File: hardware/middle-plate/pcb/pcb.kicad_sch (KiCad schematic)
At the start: 101 parts, among them J1 Conn_01x06, J2 Conn_01x06, J3 Conn_01x05, J4 Conn_01x04, SW1 MT-0-102-A101-M200-RS+PJ, SW10 TS4535TP 250GF 009, SW11 TS4535TP 250GF 009, SW2 TS4535TP 250GF 009, SW3 TS4535TP 250GF 009, SW4 TS4535TP 250GF 009, SW5 TS4535TP 250GF 009, SW6 TS4535TP 250GF 009, SW7 TS4535TP 250GF 009, SW8 TS4535TP 250GF 009, SW9 TS4535TP 250GF 009, U1 Pico, U2 RPi_Zero_2W, U3 SN74LVC1T45DBV, U4 MAX98357_breakout

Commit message: middle plate completed other than cutouts
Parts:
- added J5: Conn_01x05, Connector_JST:JST_XH_B5B-XH-A_1x05_P2.50mm_Vertical, symbol Connector_Generic:Conn_01x05
- added J6: Conn_01x04, Connector_JST:JST_XH_B4B-XH-A_1x04_P2.50mm_Vertical, symbol Connector_Generic:Conn_01x04
- added JP6, JP7: Jumper_3_Bridged12, Connector_PinHeader_1.27mm:PinHeader_1x03_P1.27mm_Vertical, symbol Jumper:Jumper_3_Bridged12
- added R3, R4: 2.7kR, PCM_Resistor_SMD_AKL:R_1206_3216Metric_Pad1.30x1.75mm_HandSolder, symbol Device:R
- added R5, R6, R7, R8, R9: 10kR, PCM_Resistor_SMD_AKL:R_1206_3216Metric_Pad1.30x1.75mm_HandSolder, symbol Device:R
- added SW12: TS4535TP 250GF 009, EasyEDA:SW-SMD_4P-L4.5-W4.5-P3.00-LS6.8, symbol EasyEDA:TS4535TP250GF009
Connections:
- net +3V3: now also JP6.1 (A), JP7.1 (A), R3.1, R4.1, R5.1, R6.1, R7.1, R8.1, R9.1; no longer U2.17 (3V3)
- net +5V: now also JP6.3 (B), JP7.3 (B)
- net ADC_IN1: now also J5.2 (Pin_2)
- net ADC_IN2: now also J5.4 (Pin_4)
- net ADC_IN3: now also J5.3 (Pin_3)
- net ADC_INT: now also U2.18 (GP24)
- net GND: now also J5.1 (Pin_1), J6.1 (Pin_1), SW12.1, SW12.2
- net IR1: now also U1.22 (GPIO17); no longer U1.1 (GPIO0)
- net IR10: now also U1.2 (GPIO1); no longer U1.12 (GPIO9)
- net IR11: now also U1.4 (GPIO2); no longer U1.14 (GPIO10)
- net IR12: now also U1.5 (GPIO3); no longer U1.15 (GPIO11)
- net IR13: now also U1.6 (GPIO4); no longer U1.16 (GPIO12)
- net IR14: now also U1.7 (GPIO5); no longer U1.17 (GPIO13)
- net IR15: now also U1.9 (GPIO6); no longer U1.19 (GPIO14)
- net IR16: now also U1.10 (GPIO7); no longer U1.20 (GPIO15)
- net IR17: now also U1.11 (GPIO8); no longer U1.34 (GPIO28_ADC2)
- net IR18: now also U1.12 (GPIO9); no longer U1.32 (GPIO27_ADC1)
- net IR19: now also U1.14 (GPIO10); no longer U1.31 (GPIO26_ADC0)
- net IR2: now also U1.21 (GPIO16); no longer U1.2 (GPIO1)
- net IR20: now also U1.15 (GPIO11); no longer U1.29 (GPIO22)
- net IR21: now also U1.16 (GPIO12); no longer U1.27 (GPIO21)
- net IR22: now also U1.17 (GPIO13); no longer U1.26 (GPIO20)
- net IR23: now also U1.19 (GPIO14); no longer U1.25 (GPIO19)
- net IR24: now also U1.20 (GPIO15); no longer U1.24 (GPIO18)
- net IR3: now also U1.24 (GPIO18); no longer U1.4 (GPIO2)
- net IR4: now also U1.25 (GPIO19); no longer U1.5 (GPIO3)
- net IR5: now also U1.26 (GPIO20); no longer U1.6 (GPIO4)
- net IR6: now also U1.27 (GPIO21); no longer U1.7 (GPIO5)
- net IR7: now also U1.32 (GPIO27_ADC1); no longer U1.9 (GPIO6)
- net IR8: now also U1.34 (GPIO28_ADC2); no longer U1.10 (GPIO7)
- net IR9: now also U1.1 (GPIO0); no longer U1.11 (GPIO8)
- net LED_SIG_3V3: now also U1.31 (GPIO26_ADC0); no longer U1.22 (GPIO17)
- net LED_SIG_DIR: now also U1.29 (GPIO22); no longer U1.21 (GPIO16), U2.36 (GP16)
- net LRC: now also U2.16 (GP23); no longer U2.37 (GP26)
- net PI_SW1: now also U2.31 (GP6), R5.2; no longer U2.15 (GP22)
- net PI_SW2: now also U2.29 (GP5), R6.2; no longer U2.27 (GP0(EEPROM_SDA))
- net PI_SW3: now also U2.27 (GP0(EEPROM_SDA)), R7.2; no longer U2.29 (GP5)
- net PI_SW4: now also U2.36 (GP16), R8.2; no longer U2.31 (GP6)
- net PWM0: now also J6.3 (Pin_3)
- net PWM1: now also J6.2 (Pin_2)
- net TOPPICO_TOGGLE.RUN: now reaches U2.7 (GP4(GPCLK0))
- net TOPPICO_TOGGLE.RUN: now also CTRL1.2 (Pin_2), SW3.3, SW3.4
- net BOTTOMPICO_EN renamed TOPPICO_TOGGLE.EN
- net TOPPICO_TOGGLE.EN: now also CTRL1.1 (Pin_1)
- removed net BOTTOMPICO_RUN: SW3.3, SW3.4, U2.13 (GP27)
- removed net EN: CTRL1.1 (Pin_1), CTRL2.2 (Pin_2), U1.37 (3V3_EN)
- net MIDPICO_EN renamed MIDPICO_TOGGLE.EN
- net MIDPICO_TOGGLE.EN: now also U1.37 (3V3_EN)
- net MIDPICO_RUN renamed MIDPICO_TOGGLE.RUN
- net MIDPICO_TOGGLE.RUN: now also U1.30 (RUN)
- net PCM_CLK renamed PCM.CLK
- net PCM_DIN renamed PCM.DIN
- net PCM.DIN: now also J3.2 (Pin_2); no longer J3.4 (Pin_4)
- net PCM_DOUT renamed PCM.DOUT
- net PCM_FS renamed PCM.FS
- net PCM.FS: now also J3.4 (Pin_4); no longer J3.2 (Pin_2)
- removed net RUN: CTRL1.2 (Pin_2), CTRL2.1 (Pin_1), U1.30 (RUN)
- net RX renamed PI_UART.RX
- net PI_UART.RX: now also CTRL2.4 (Pin_4); no longer CTRL2.3 (Pin_3)
- net SCL renamed PI_I2C.SCL
- net PI_I2C.SCL: now also J4.2 (Pin_2), R4.2; no longer J4.3 (Pin_3)
- net SDA renamed PI_I2C.SDA
- net PI_I2C.SDA: now also J4.3 (Pin_3), R3.2; no longer J4.2 (Pin_2)
- net SPI0_CE0 renamed RPI_SPI0.MOSI
- net RPI_SPI0.MOSI: now also J2.5 (Pin_5), U2.19 (GP10(SPI0_MOSI)); no longer U2.24 (GP8(SPI0_CE0))
- net SPI0_CE1 renamed RPI_SPI0.SCS1
- net RPI_SPI0.SCS1: now also J2.2 (Pin_2); no longer J2.5 (Pin_5)
- net SPI0_MISO renamed RPI_SPI0.SCLK
- net RPI_SPI0.SCLK: now also U2.23 (GP11(SPI0_SCLK)); no longer U2.21 (GP9(SPI0_MISO))
- removed net SPI0_MOSI: J1.2 (Pin_2), J2.2 (Pin_2), U2.19 (GP10(SPI0_MOSI))
- net SPI0_SCLK renamed RPI_SPI0.MISO
- net RPI_SPI0.MISO: now also U2.21 (GP9(SPI0_MISO)); no longer U2.23 (GP11(SPI0_SCLK))
- net TOPPICO_EN renamed BOTTOMPICO_TOGGLE.EN
- net BOTTOMPICO_TOGGLE.EN: now also CTRL2.2 (Pin_2), U2.13 (GP27); no longer U2.16 (GP23)
- net TOPPICO_RUN renamed BOTTOMPICO_TOGGLE.RUN
- net BOTTOMPICO_TOGGLE.RUN: now also CTRL2.1 (Pin_1), U2.15 (GP22); no longer U2.18 (GP24)
- net TX renamed PI_UART.TX
- net PI_UART.TX: now also CTRL2.3 (Pin_3); no longer CTRL2.4 (Pin_4)
- new net: J6.4 (Pin_4), JP7.2 (C)
- new net: J5.5 (Pin_5), JP6.2 (C)
- new net PI_SW5: R9.2, SW12.3, SW12.4, U2.37 (GP26)
- new net RPI_SPI0.SCS0: J1.2 (Pin_2), U2.24 (GP8(SPI0_CE0))
- no-connect marks 27 -> 28
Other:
- note added: "A bunch of pushbuttons for centralised hardware and software control. RPi control pushbuttons have a pullup resistor. Make sure it can only sink 0.5mA (at least 7kOhm)."
- note added: "pullup resistors for I2C. Internal pullups of the RPi Zero 2W are too weak to reliably drive 400kHz I2C. Adjust values accordingly, 2.7K is probably safe. DNP and lower speeds if necessary. Lower values can be used if capacitance is too high. And of course, avoid running I2C on wires."
- note removed: "A bunch of pushbuttons for centralised hardware and software control."
- moved on the sheet: CTRL1, CTRL2, H1, H10, H11, H12, H13, H14, H15, H16, H2, H3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

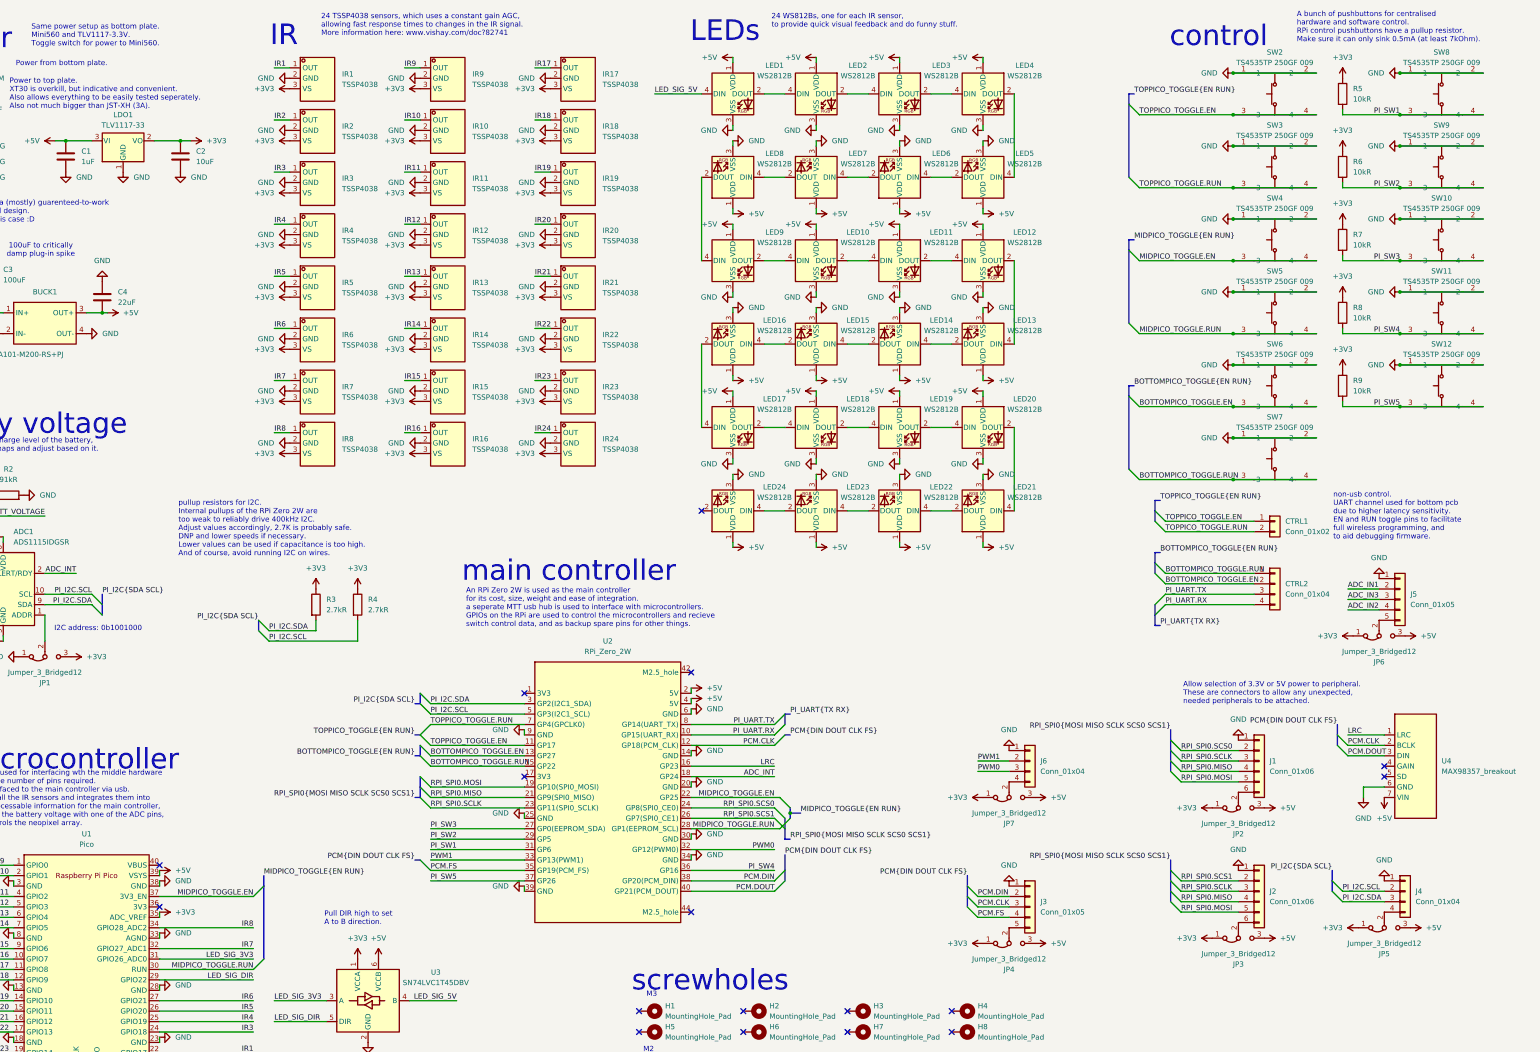
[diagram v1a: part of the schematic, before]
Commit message: changed some reference designators, and cleaned up schematics
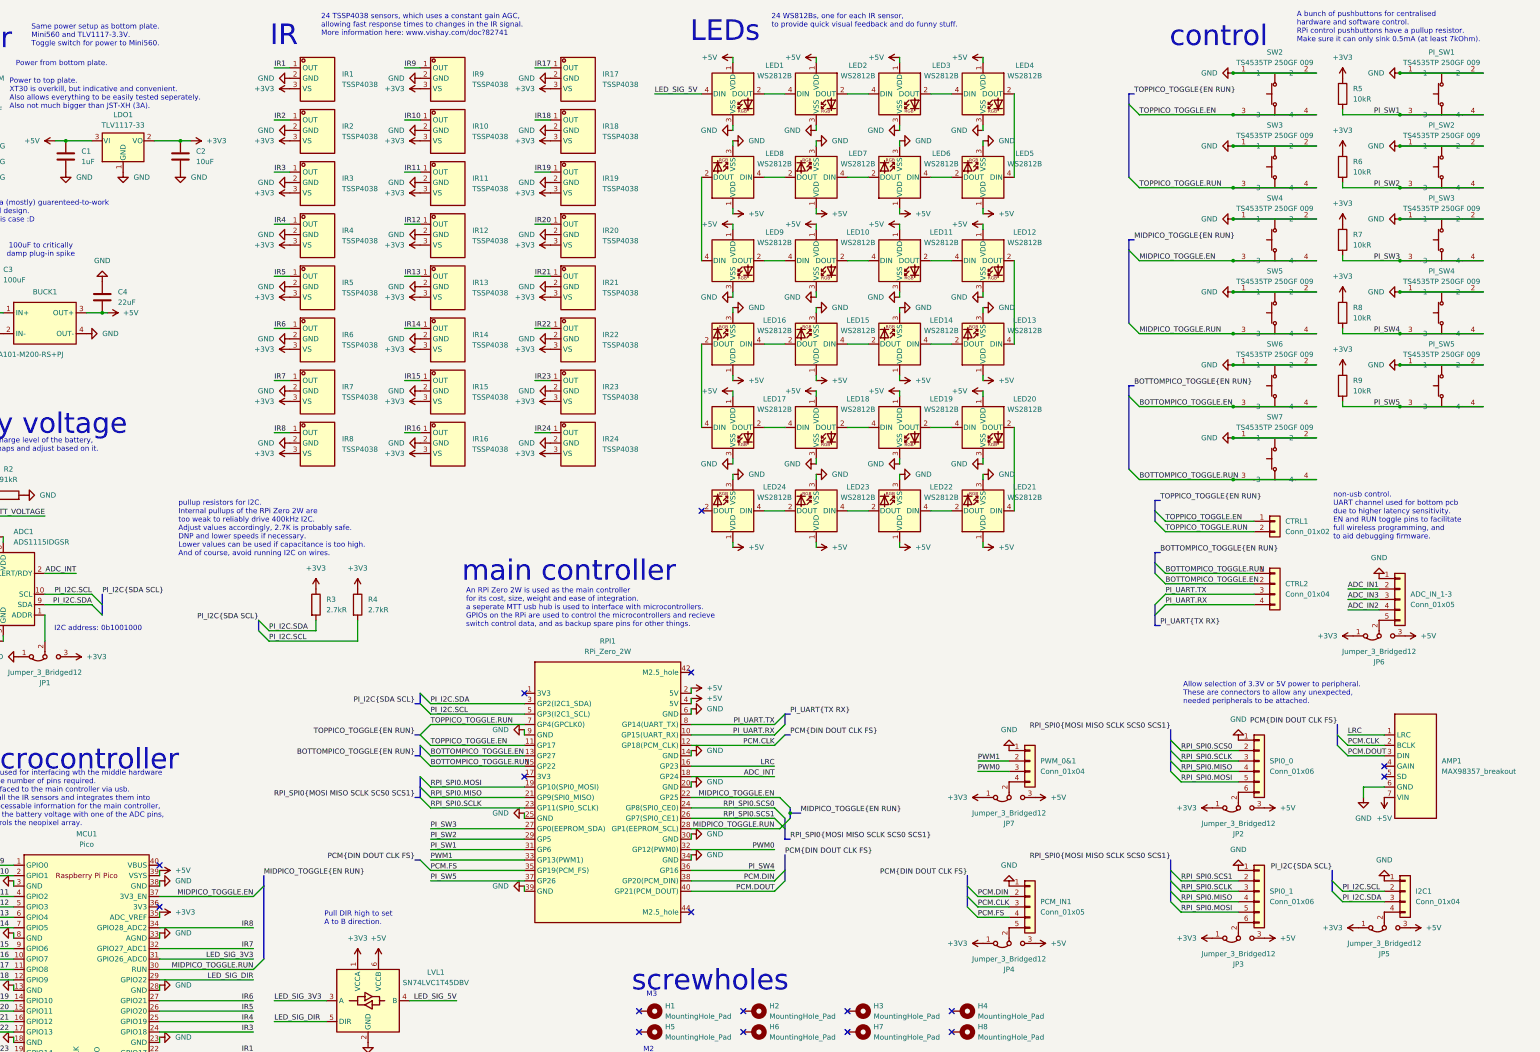
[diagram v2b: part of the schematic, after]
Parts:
- renumbered J5 to ADC_IN_1-3, U4 to AMP1, J4 to I2C1, U3 to LVL1, U1 to MCU1, J3 to PCM_IN1, SW8 to PI_SW1, SW9 to PI_SW2, SW10 to PI_SW3, SW11 to PI_SW4, SW12 to PI_SW5, J6 to PWM_0&1, U2 to RPI1, J1 to SPI0_0, J2 to SPI0_1
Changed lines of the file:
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@@
 		(dnp no)
 		(fields_autoplaced yes)
-		(property "Reference" "U2"
+		(property "Reference" "RPI1"
 			(at 185.42 168.91 0)
 			(effects
@@
 			(project ""
 				(path "/9bb3e9c6-12db-4b47-aa39-b193ca752b9a"
-					(reference "U2")
+					(reference "RPI1")
 					(unit 1)
 				)
@@
 		(dnp no)
 		(fields_autoplaced yes)
-		(property "Reference" "U3"
+		(property "Reference" "LVL1"
 			(at 143.51 249.6055 0)
 			(effects
@@
 			(project "pcb"
 				(path "/9bb3e9c6-12db-4b47-aa39-b193ca752b9a"
-					(reference "U3")
+					(reference "LVL1")
 					(unit 1)
 				)
@@
 		(dnp no)
 		(fields_autoplaced yes)
-		(property "Reference" "U1"
+		(property "Reference" "MCU1"
 			(at 58.42 215.9 0)
 			(effects
@@
 			(project ""
 				(path "/9bb3e9c6-12db-4b47-aa39-b193ca752b9a"
-					(reference "U1")
+					(reference "MCU1")
 					(unit 1)
 				)
@@
 		(dnp no)
 		(fields_autoplaced yes)
-		(property "Reference" "SW12"
+		(property "Reference" "PI_SW5"
 			(at 388.62 96.52 0)
 			(effects
@@
 			(project "pcb"
 				(path "/9bb3e9c6-12db-4b47-aa39-b193ca752b9a"
-					(reference "SW12")
+					(reference "PI_SW5")
 					(unit 1)
 				)
@@
 		(dnp no)
 		(fields_autoplaced yes)
-		(property "Reference" "J6"
+		(property "Reference" "PWM_0&1"
 			(at 290.83 198.1199 0)
 			(effects
@@
 			(project "pcb"
 				(path "/9bb3e9c6-12db-4b47-aa39-b193ca752b9a"
-					(reference "J6")
+					(reference "PWM_0&1")
 					(unit 1)
 				)
@@
 		(dnp no)
 		(fields_autoplaced yes)
-		(property "Reference" "J3"
+		(property "Reference" "PCM_IN1"
 			(at 290.83 232.4099 0)
 			(effects
@@
 			(project ""
 				(path "/9bb3e9c6-12db-4b47-aa39-b193ca752b9a"
-					(reference "J3")
+					(reference "PCM_IN1")
 					(unit 1)
 				)
@@
 		(dnp no)
 		(fields_autoplaced yes)
-		(property "Reference" "J4"
+		(property "Reference" "I2C1"
 			(at 382.27 229.8699 0)
 			(effects
@@
 			(project ""
 				(path "/9bb3e9c6-12db-4b47-aa39-b193ca752b9a"
-					(reference "J4")
+					(reference "I2C1")
 					(unit 1)
 				)
@@
 		(dnp no)
 		(fields_autoplaced yes)
-		(property "Reference" "SW11"
+		(property "Reference" "PI_SW4"
 			(at 388.62 78.74 0)
 			(effects
@@
 			(project "middle-plate"
 				(path "/9bb3e9c6-12db-4b47-aa39-b193ca752b9a"
-					(reference "SW11")
+					(reference "PI_SW4")
 					(unit 1)
 				)
@@
 		(dnp no)
 		(fields_autoplaced yes)
-		(property "Reference" "SW9"
+		(property "Reference" "PI_SW2"
 			(at 388.62 43.18 0)
 			(effects
@@
 			(project "middle-plate"
 				(path "/9bb3e9c6-12db-4b47-aa39-b193ca752b9a"
-					(reference "SW9")
+					(reference "PI_SW2")
 					(unit 1)
 				)
@@
 		(dnp no)
 		(fields_autoplaced yes)
-		(property "Reference" "J1"
+		(property "Reference" "SPI0_0"
 			(at 346.71 198.1199 0)
 			(effects
@@
 			(project ""
 				(path "/9bb3e9c6-12db-4b47-aa39-b193ca752b9a"
-					(reference "J1")
+					(reference "SPI0_0")
 					(unit 1)
 				)
@@
 		(dnp no)
 		(fields_autoplaced yes)
-		(property "Reference" "SW10"
+		(property "Reference" "PI_SW3"
 			(at 388.62 60.96 0)
 			(effects
@@
 			(project "middle-plate"
 				(path "/9bb3e9c6-12db-4b47-aa39-b193ca752b9a"
-					(reference "SW10")
+					(reference "PI_SW3")
 					(unit 1)
 				)
@@
 		(dnp no)
 		(fields_autoplaced yes)
-		(property "Reference" "J2"
+		(property "Reference" "SPI0_1"
 			(at 346.71 229.8699 0)
 			(effects
@@
 			(project "middle-plate"
 				(path "/9bb3e9c6-12db-4b47-aa39-b193ca752b9a"
-					(reference "J2")
+					(reference "SPI0_1")
 					(unit 1)
 				)
@@
 		(dnp no)
 		(fields_autoplaced yes)
-		(property "Reference" "U4"
+		(property "Reference" "AMP1"
 			(at 388.62 198.1199 0)
 			(effects
@@
 			(project ""
 				(path "/9bb3e9c6-12db-4b47-aa39-b193ca752b9a"
-					(reference "U4")
+					(reference "AMP1")
 					(unit 1)
 				)
@@
 		(dnp no)
 		(fields_autoplaced yes)
-		(property "Reference" "SW8"
+		(property "Reference" "PI_SW1"
 			(at 388.62 25.4 0)
 			(effects
@@
 			(project "middle-plate"
 				(path "/9bb3e9c6-12db-4b47-aa39-b193ca752b9a"
-					(reference "SW8")
+					(reference "PI_SW1")
 					(unit 1)
 				)
@@
 		(dnp no)
 		(fields_autoplaced yes)
-		(property "Reference" "J5"
+		(property "Reference" "ADC_IN_1-3"
 			(at 381 157.4799 0)
 			(effects
@@
 			(project "pcb"
 				(path "/9bb3e9c6-12db-4b47-aa39-b193ca752b9a"
-					(reference "J5")
+					(reference "ADC_IN_1-3")
 					(unit 1)
 				)

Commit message: funny thing
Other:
- note added: "What could this sneaky amp be possibly doing? Have any grapes?"
- moved on the sheet: AMP1
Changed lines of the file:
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@@
 	)
 	(no_connect
-		(at 374.65 201.93)
+		(at 261.62 170.18)
 	)
 	(no_connect
@@
 	)
 	(no_connect
-		(at 374.65 199.39)
+		(at 261.62 167.64)
 	)
 	(no_connect
@@
 	)
 	(bus_entry
-		(at 363.22 191.77)
+		(at 250.19 160.02)
 		(size 2.54 2.54)
 		(stroke
@@
 	)
 	(bus_entry
-		(at 363.22 194.31)
+		(at 250.19 162.56)
 		(size 2.54 2.54)
 		(stroke
@@
 	(wire
 		(pts
-			(xy 365.76 196.85) (xy 374.65 196.85)
+			(xy 252.73 165.1) (xy 261.62 165.1)
 		)
 		(stroke
@@
 	(wire
 		(pts
-			(xy 369.57 204.47) (xy 369.57 207.01)
+			(xy 256.54 172.72) (xy 256.54 175.26)
 		)
 		(stroke
@@
 	(bus
 		(pts
-			(xy 363.22 189.23) (xy 363.22 191.77)
+			(xy 250.19 157.48) (xy 250.19 160.02)
 		)
 		(stroke
@@
 	(wire
 		(pts
-			(xy 369.57 204.47) (xy 374.65 204.47)
+			(xy 256.54 172.72) (xy 261.62 172.72)
 		)
 		(stroke
@@
 	(bus
 		(pts
-			(xy 363.22 191.77) (xy 363.22 194.31)
+			(xy 250.19 160.02) (xy 250.19 162.56)
 		)
 		(stroke
@@
 	(wire
 		(pts
-			(xy 365.76 191.77) (xy 374.65 191.77)
+			(xy 252.73 160.02) (xy 261.62 160.02)
 		)
 		(stroke
@@
 	(wire
 		(pts
-			(xy 365.76 194.31) (xy 374.65 194.31)
+			(xy 252.73 162.56) (xy 261.62 162.56)
 		)
 		(stroke
@@
 		)
 	)
+	(text "What could this sneaky\namp be possibly doing?\nHave any grapes?"
+		(exclude_from_sim no)
+		(at 276.098 158.496 0)
+		(effects
+			(font
+				(size 1.27 1.27)
+			)
+			(justify left)
+		)
+	)
 	(text "MINI560 reg, to have a (mostly) guarenteed-to-work\nand replacable-if-fried design.\n5A is not overkill in this case :D"
 		(exclude_from_sim no)
@@
 	)
 	(label "PCM{DIN DOUT CLK FS}"
-		(at 363.22 189.23 180)
+		(at 250.19 157.48 180)
 		(fields_autoplaced yes)
 		(effects
@@
 	)
 	(label "PCM.CLK"
-		(at 365.76 194.31 0)
+		(at 252.73 162.56 0)
 		(fields_autoplaced yes)
 		(effects
@@
 	)
 	(label "LRC"
-		(at 365.76 191.77 0)
+		(at 252.73 160.02 0)
 		(fields_autoplaced yes)
 		(effects
@@
 	)
 	(label "PCM.DOUT"
-		(at 365.76 196.85 0)
+		(at 252.73 165.1 0)
 		(fields_autoplaced yes)
 		(effects
@@
 	(symbol
 		(lib_id "power:GND")
-		(at 369.57 207.01 0)
+		(at 256.54 175.26 0)
 		(unit 1)
 		(exclude_from_sim no)
@@
 		(fields_autoplaced yes)
 		(property "Reference" "#PWR0161"
-			(at 369.57 213.36 0)
+			(at 256.54 181.61 0)
 			(effects
 				(font
@@
 		)
 		(property "Value" "GND"
-			(at 369.57 212.09 0)
+			(at 256.54 180.34 0)
 			(effects
 				(font
@@
 		)
 		(property "Footprint" ""
-			(at 369.57 207.01 0)
+			(at 256.54 175.26 0)
 			(effects
 				(font
@@
 		)
 		(property "Datasheet" ""
-			(at 369.57 207.01 0)
+			(at 256.54 175.26 0)
 			(effects
 				(font
@@
 		)
 		(property "Description" "Power symbol creates a global label with name \"GND\" , ground"
-			(at 369.57 207.01 0)
+			(at 256.54 175.26 0)
 			(effects
 				(font
@@
 	(symbol
 		(lib_id "custom:MAX98357_breakout_no_mountingholes")
-		(at 379.73 199.39 0)
+		(at 266.7 167.64 0)
 		(unit 1)
 		(exclude_from_sim no)
@@
 		(fields_autoplaced yes)
 		(property "Reference" "AMP1"
-			(at 388.62 198.1199 0)
+			(at 275.59 166.3699 0)
 			(effects
 				(font
@@
 		)
 		(property "Value" "MAX98357_breakout"
-			(at 388.62 200.6599 0)
+			(at 275.59 168.9099 0)
 			(effects
 				(font
@@
 		)
 		(property "Footprint" "custom:MAX98357_breakout_no_mountingholes"
-			(at 379.73 199.39 0)
+			(at 266.7 167.64 0)
 			(effects
 				(font
@@
 		)
 		(property "Datasheet" ""
-			(at 379.73 199.39 0)
+			(at 266.7 167.64 0)
 			(effects
 				(font
@@
 		)
 		(property "Description" ""
-			(at 379.73 199.39 0)
+			(at 266.7 167.64 0)
 			(effects
 				(font
@@
 	(symbol
 		(lib_id "power:+5V")
-		(at 374.65 207.01 180)
+		(at 261.62 175.26 180)
 		(unit 1)
 		(exclude_from_sim no)
@@
 		(fields_autoplaced yes)
 		(property "Reference" "#PWR0162"
-			(at 374.65 203.2 0)
+			(at 261.62 171.45 0)
 			(effects
 				(font
@@
 		)
 		(property "Value" "+5V"
-			(at 374.65 212.09 0)
+			(at 261.62 180.34 0)
 			(effects
 				(font
@@
 		)
 		(property "Footprint" ""
-			(at 374.65 207.01 0)
+			(at 261.62 175.26 0)
 			(effects
 				(font
@@
 		)
 		(property "Datasheet" ""
-			(at 374.65 207.01 0)
+			(at 261.62 175.26 0)
 			(effects
 				(font
@@
 		)
 		(property "Description" "Power symbol creates a global label with name \"+5V\""
-			(at 374.65 207.01 0)
+			(at 261.62 175.26 0)
 			(effects
 				(font

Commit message: fixed middle plate and added stuff to gitignore
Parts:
- added H17, H18, H19, H20, H21: MountingHole_Pad, MountingHole:MountingHole_2.2mm_M2_Pad_Via, symbol Mechanical:MountingHole_Pad
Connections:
- no-connect marks 28 -> 33
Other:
- moved on the sheet: H1, H10, H11, H12, H13, H14, H15, H16, H2, H3, H4, H5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
